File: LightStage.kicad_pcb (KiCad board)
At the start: 2 copper layers, 161 parts, among them J1 Conn_01x02_Male, J10 Conn_01x02_Male, J11 Conn_01x02_Male, J12 Conn_01x02_Male, J13 Conn_01x02_Male, J14 Conn_01x02_Male, J15 Conn_01x02_Male, J16 Conn_01x02_Male, J17 Conn_01x02_Male, J18 Conn_01x02_Male, J19 Conn_01x02_Male, J2 Conn_01x02_Male, J20 Conn_01x02_Male, J21 Conn_01x02_Male, J22 Conn_01x02_Male, J23 Conn_01x02_Male, J24 Conn_01x02_Male, J25 Conn_01x02_Male, J26 Conn_01x02_Male, J3 Conn_01x02_Male, J4 Conn_01x02_Male, J5 Conn_01x02_Male, J6 Conn_01x02_Male, J7 Conn_01x02_Male, J8 Conn_01x02_Male, J9 Conn_01x02_Male, U1 PCA9685PW, U10 TPS92200D2DDCR, U11 TPS92200D2DDCR, U12 TPS92200D2DDCR, U13 TPS92200D2DDCR, U14 TPS92200D2DDCR, U15 TPS92200D2DDCR, U16 TPS92200D2DDCR, U17 TPS92200D2DDCR, U18 TPS92200D2DDCR, U19 TPS92200D2DDCR, U2 LM78L05ACM_NOPB, U3 TPS92200D2DDCR, U4 TPS92200D2DDCR, U5 TPS92200D2DDCR, U6 TPS92200D2DDCR, U7 TPS92200D2DDCR, U8 TPS92200D2DDCR, U9 TPS92200D2DDCR

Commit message: Light Stage version 2
Light Stage
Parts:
- removed the C10 at (63.5, 67.3)
- removed the C14 at (64.8, 48.3)
- removed the C16 at (63.5, 63.5)
- removed the C20 at (82.5, 49.5)
- removed the C21 at (82.5, 67.3)
- removed C24, C42, C43, C44, C45, C46, C62, C63, C64, C65, C66: 10uF, Capacitor_SMD:C_1206_3216Metric_Pad1.33x1.80mm_HandSolder
- removed the C25 at (82.5, 63.5)
- removed the C28 at (134.6, -20.3)
- removed the C29 at (121.2, -23.2)
- removed the C3 at (68.6, 73.7)
- removed the C30 at (112.0, -12.3)
- removed the C31 at (116.6, -19.4)
- removed the C32 at (121.2, -26.6)
- removed the C33 at (130.4, -33.7)
- removed the C34 at (112.0, -8.92)
- removed the C35 at (122.6, -19.9)
- removed the C37 at (136.4, -33.7)
- removed C4, C52, C53, C54, C55, C56: 0.1uF, Capacitor_SMD:C_1206_3216Metric_Pad1.33x1.80mm_HandSolder
- removed the C6 at (64.8, 17.8)
- removed the C8 at (64.8, 52.1)
- removed the J2 at (87.6, 25.4)
- removed J21, J22, J23, J24, J25, J26, J3: Conn_01x02_Male, Connector_PinSocket_2.54mm:PinSocket_1x02_P2.54mm_Vertical
- removed the L7 at (147.0, -12.9)
- removed the R10 at (83.8, 21.2)
- removed the R17 at (151.6, -13.7)
- removed the R4 at (82.5, 34.3)
- removed the R5 at (69.8, 35.6)
- removed the R6 at (69.8, 34.3)
- removed the R7 at (69.8, 33.0)
- removed the R8 at (69.8, 31.8)
- removed the R9 at (69.8, 30.5)
- removed the U2 at (73.0, 71.1)
- removed the U9 at (154.1, -29.7)
- added ?: , KicadFootPrints:Logo_NoPo_kicad, F.Cu at (38.1, 141.6)
- added J7: , 781710004 Pico-EZmate:781710004, F.Cu at (90.4, 47.2)
- added M1: MountingHole_4.3mm_M4, MountingHole:MountingHole_4.3mm_M4, F.Cu at (36.2, 46.4)
- added M2: MountingHole_4.3mm_M4, MountingHole:MountingHole_4.3mm_M4, F.Cu at (116.2, 146.1)
- added RN1: 4609M-101-103LF, SamacSys_Parts:4609X, F.Cu at (70.6, 97.0)
- added U1: LM78L05ACM_NOPB, footprints:LM78L05ACM&slash_NOPB, F.Cu at (68.1, 66.5)
- D1: footprint LED_SMD:LED_0201_0603Metric_Pad0.64x0.40mm_HandSolder -> LED_SMD:LED_0402_1005Metric_Pad0.77x0.64mm_HandSolder
- J1: value Conn_01x02_Male -> Conn_02x07_Odd_Even; footprint Connector_PinSocket_2.54mm:PinSocket_1x02_P2.54mm_Vertical -> Connector_PinHeader_2.54mm:PinHeader_2x07_P2.54mm_Vertical_SMD
- J10, J11, J12, J13, J14, J16, J17, J18, J19, J4, J5, J6, J8, J9: value Conn_01x02_Male -> (none); footprint Connector_PinSocket_2.54mm:PinSocket_1x02_P2.54mm_Vertical -> 781710004 Pico-EZmate:781710004
- J15: value Conn_01x02_Male -> (none); footprint Connector_PinHeader_2.54mm:PinHeader_1x02_P2.54mm_Vertical -> 781710004 Pico-EZmate:781710004
- J2: renamed from J7; footprint Connector_PinHeader_2.54mm:PinHeader_1x02_P2.54mm_Vertical -> SamacSys_Parts:Molex_26013114; moved to B.Cu
- J20: value Conn_01x02_Male -> 781710004; footprint Connector_PinSocket_2.54mm:PinSocket_1x02_P2.54mm_Vertical -> 781710004 Pico-EZmate:781710004
- U10: renamed from U11; value TPS92200D2DDCR -> (none)
- U11: renamed from U12; value TPS92200D2DDCR -> (none)
- U12: renamed from U13; value TPS92200D2DDCR -> (none)
- U13: renamed from U14; value TPS92200D2DDCR -> (none)
- U14: renamed from U15; value TPS92200D2DDCR -> (none)
- U15: renamed from U16; value TPS92200D2DDCR -> (none)
- U16: renamed from U17; value TPS92200D2DDCR -> (none)
- U17: renamed from U18; value TPS92200D2DDCR -> (none)
- U18: renamed from U19; value TPS92200D2DDCR -> (none)
- U2: renamed from U7; value TPS92200D2DDCR -> (none)
- U3: renamed from U8; value TPS92200D2DDCR -> (none)
- U5: renamed from U4; value TPS92200D2DDCR -> (none)
- U6: renamed from U5; value TPS92200D2DDCR -> (none)
- U7: renamed from U6; value TPS92200D2DDCR -> (none)
- U8: renamed from U3; value TPS92200D2DDCR -> (none)
- U9: renamed from U10; value TPS92200D2DDCR -> (none)
- moved C25 176.5 mm to (106.2, 136.1), turned to 270 degrees
- moved C20 166.2 mm to (87.1, 130.0)
- moved C26 164.3 mm to (92.2, 136.7), turned to 90 degrees
- moved J20 159.9 mm to (41.1, 119.9), turned to 270 degrees
- moved J18 159.8 mm to (37.5, 103.5), turned to 270 degrees
- moved L8 159.3 mm to (92.2, 131.3), turned to 270 degrees
- moved R11 157.1 mm to (87.1, 138.9)
- moved R12 156.1 mm to (106.2, 122.4), turned to 90 degrees
- moved U11 151.0 mm to (102.4, 122.4), turned to 180 degrees
- moved U9 151.0 mm to (101.1, 135.1), turned to 90 degrees
- moved L9 150.4 mm to (98.3, 117.3)
- moved U10 148.5 mm to (87.1, 135.1), turned to 90 degrees
- moved R10 148.2 mm to (101.1, 138.9)
- moved L11 147.0 mm to (42.7, 60.4), turned to 90 degrees
- moved C18 146.9 mm to (101.1, 130.0)
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- renumbered C2 to C1, C11 to C10, C12 to C11, C13 to C12, C5 to C13, C17 to C14, C18 to C15, C19 to C16, C7 to C17, C36 to C18, C9 to C2, C38 to C20, C39 to C21, C40 to C22, C41 to C23, C47 to C25, C48 to C26, C49 to C27, C50 to C28, C51 to C29, C15 to C3, C57 to C30, C58 to C31, C59 to C32, C60 to C33, C61 to C34, C67 to C35, C68 to C36, C69 to C37, C70 to C38, C71 to C39, C1 to C5, C22 to C6, C23 to C7, C26 to C8, C27 to C9, L5 to L1, L11 to L10, L12 to L11, L13 to L12, L14 to L13, L15 to L14, L16 to L15, L17 to L16, L6 to L2, L2 to L3, L3 to L4, L4 to L5, L1 to L6, L8 to L7, L9 to L8, L10 to L9, R18 to R10, R19 to R11, R20 to R12, R21 to R13, R22 to R14, R23 to R15, R24 to R16, R25 to R17, R26 to R18, R27 to R19, R15 to R4, R16 to R5, R12 to R6, R13 to R7, R14 to R8, R11 to R9, U1 to U4
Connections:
- C29 pad 1: p_LED5 -> p_LED15
- J1 pad 1: A0 -> 5V
- J1 pad 2: 5V -> A0
- J10 pad 1: OE -> n_LED7
- J10 pad 2: 5V -> Net-(J10-Pad2)
- J11 pad 1: p_LED2 -> n_LED8
- J11 pad 2: n_LED2 -> Net-(J11-Pad2)
- J12 pad 1: p_LED1 -> n_LED9
- J12 pad 2: n_LED1 -> Net-(J12-Pad2)
- J13 pad 1: p_LED3 -> n_LED4
- J13 pad 2: n_LED3 -> Net-(J13-Pad2)
- J14 pad 1: p_LED5 -> n_LED5
- J14 pad 2: n_LED5 -> Net-(J14-Pad2)
- J15 pad 1: SDA -> n_LED6
- J15 pad 2: SCL -> Net-(J15-Pad2)
- J16 pad 1: p_LED15 -> p_LED1
- J16 pad 2: n_LED15 -> Net-(J16-Pad2)
- J17 pad 1: p_LED7 -> p_LED2
- J17 pad 2: n_LED7 -> Net-(J17-Pad2)
- J18 pad 1: p_LED6 -> p_LED3
- J18 pad 2: n_LED6 -> Net-(J18-Pad2)
- J19 pad 1: p_LED8 -> p_LED0
- J19 pad 2: n_LED8 -> Net-(J19-Pad2)
- J20 pad 1: p_LED9 -> SDA
- J20 pad 2: n_LED9 -> Net-(J20-Pad2)
- J4 pad 1: A3 -> n_LED14
- J4 pad 2: 5V -> Net-(J4-Pad2)
- J5 pad 1: A4 -> n_LED15
- J5 pad 2: 5V -> Net-(J5-Pad2)
- J6 pad 1: A5 -> n_LED11
- J6 pad 2: 5V -> Net-(J6-Pad2)
- J8 pad 1: p_LED4 -> n_LED13
- J8 pad 2: n_LED4 -> Net-(J8-Pad2)
- J9 pad 1: p_LED0 -> n_LED10
- J9 pad 2: n_LED0 -> Net-(J9-Pad2)
- L11 pad 2: p_LED5 -> p_LED15
- R14 pad 1: n_LED5 -> n_LED15
- U11 pad 2: PWM3 -> PWM8
- U13 pad 1: n_LED5 -> n_LED15
- U13 pad 2: PWM5 -> PWM15
- U4 pad 12: Net-(U1-Pad12) -> PWM6
- U4 pad 13: Net-(U1-Pad13) -> PWM7
- U4 pad 15: Net-(U1-Pad15) -> PWM8
- U4 pad 16: Net-(U1-Pad16) -> PWM9
- U4 pad 17: Net-(U1-Pad17) -> PWM10
- U4 pad 18: Net-(U1-Pad18) -> PWM11
- U4 pad 19: Net-(U1-Pad19) -> PWM12
- U4 pad 20: Net-(U1-Pad20) -> PWM13
- U4 pad 21: Net-(U1-Pad21) -> PWM14
- U4 pad 22: Net-(U1-Pad22) -> PWM15
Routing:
- net 24V: track 120.2 -> 742.8 mm, vias 0 -> 19
- net SDA: track 4.41 -> 81.9 mm, vias 0 -> 4
- net PWM15: track 0.00 -> 65.1 mm
- net SCL: track 4.41 -> 66.6 mm, vias 0 -> 2
- net PWM14: track 0.00 -> 61.2 mm, vias 0 -> 2
- net PWM13: track 0.00 -> 58.9 mm, vias 0 -> 4
- net PWM12: track 0.00 -> 58.8 mm, vias 0 -> 2
- net 5V: track 44.7 -> 103.5 mm, vias 0 -> 5
- net PWM2: track 0.00 -> 56.5 mm, vias 0 -> 2
- net PWM4: track 0.00 -> 52.8 mm
- net PWM7: track 0.00 -> 45.9 mm, vias 0 -> 2
- net PWM3: track 0.00 -> 44.6 mm
- net PWM0: track 0.00 -> 43.8 mm, vias 0 -> 2
- net PWM5: track 0.00 -> 39.9 mm, vias 0 -> 2
- net PWM1: track 0.00 -> 39.5 mm, vias 0 -> 2
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- added copper zone on B.Cu, net GND
- added copper zone on F.Cu, net GND
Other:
- board outline added: 91.1 x 111 mm
- board text added: "24V"
- board text added: "Cluster-A"
- board text added: "Cluster-B"
- board text added: "Cluster-C"
- board text added: "Cluster-D"
- board text added: "GND"
- board text added: "I2C only"
- board text added: "MP"
- board text added: "Nanotechnologies"
- board text added: "Power -24V 11A"
- board text added: "Version-1"

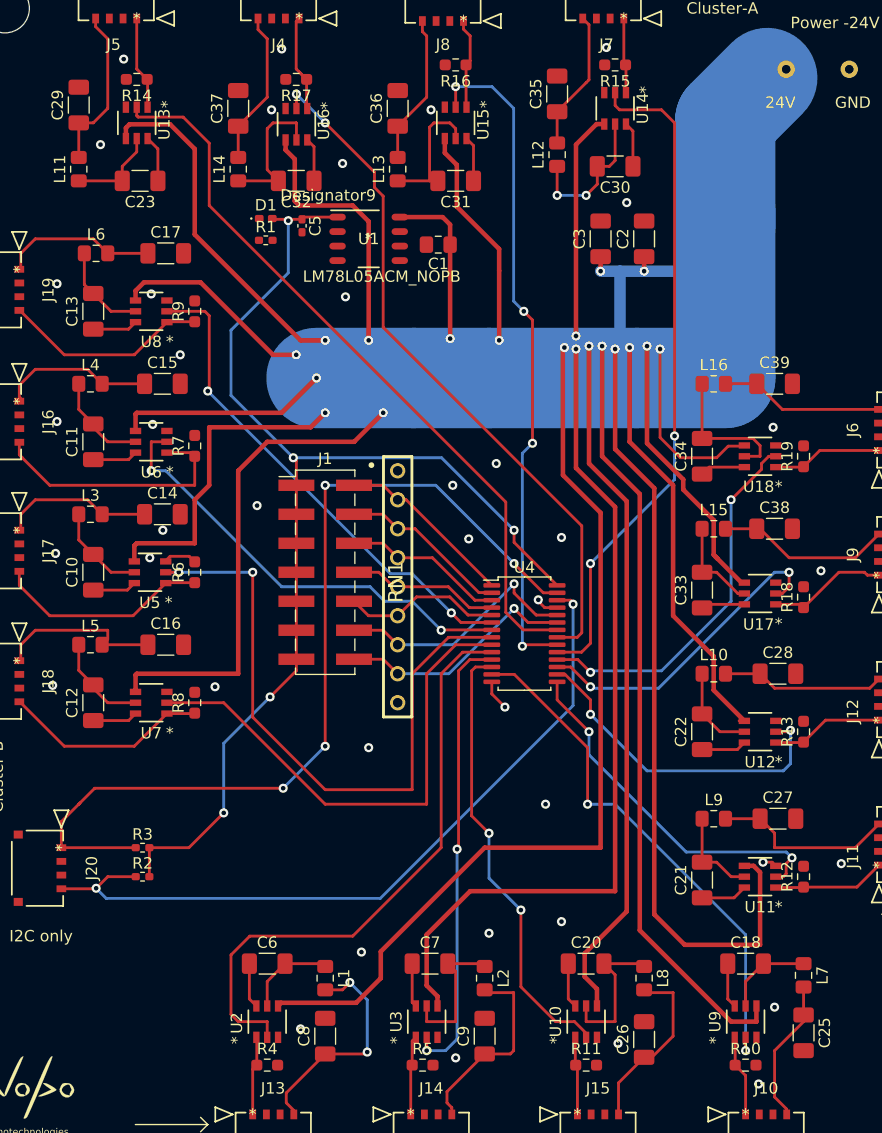
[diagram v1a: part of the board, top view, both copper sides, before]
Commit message: LightStage Version 2 with all comp on Top
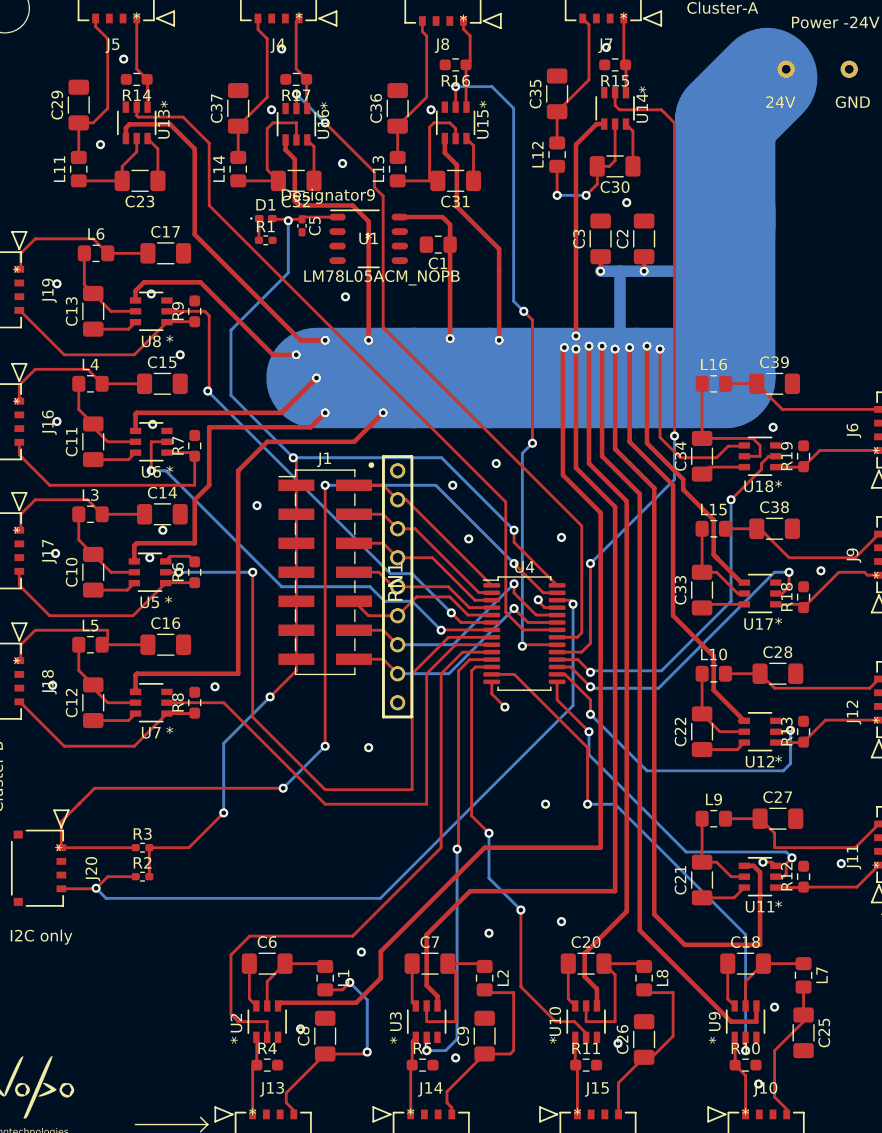
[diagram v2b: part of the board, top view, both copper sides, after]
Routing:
- net Net-(D1-Pad1): track 0.00 -> 1.92 mm

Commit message: The updated kicad drawings
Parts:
- removed ?: , KicadFootPrints:Logo_NoPo_kicad
- removed M1, M2: MountingHole_4.3mm_M4, MountingHole:MountingHole_4.3mm_M4
- added  : , KicadFootPrints:Logo_NoPo_kicad, F.Cu at (38.6, 141.7)
- C5: footprint Capacitor_SMD:C_0402_1005Metric_Pad0.74x0.62mm_HandSolder -> Capacitor_SMD:C_1206_3216Metric_Pad1.33x1.80mm_HandSolder
- moved C5 1.21 mm to (62.5, 66.6)
- moved D1 0.51 mm to (59.1, 64.3)
- moved R1 0.51 mm to (59.1, 66.2)
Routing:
- net 5V: track 103.5 -> 107.5 mm
- net GND: track 8.92 -> 12.6 mm
- net 24V: track 742.8 -> 740.1 mm
